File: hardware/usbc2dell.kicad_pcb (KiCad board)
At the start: 2 copper layers, 39.5 x 26.5 mm, 27 parts, among them J1 TYPE-C-31-M-17, J2 WJ15EDGRC-3.81-3P, Q1 DOD50P06, Q2 MMBT5551, SW1 DSWB04LHGET, U1 ATtiny1616-M, U2 FUSB302BMPX, U3 L7805, U4 SRV05-4

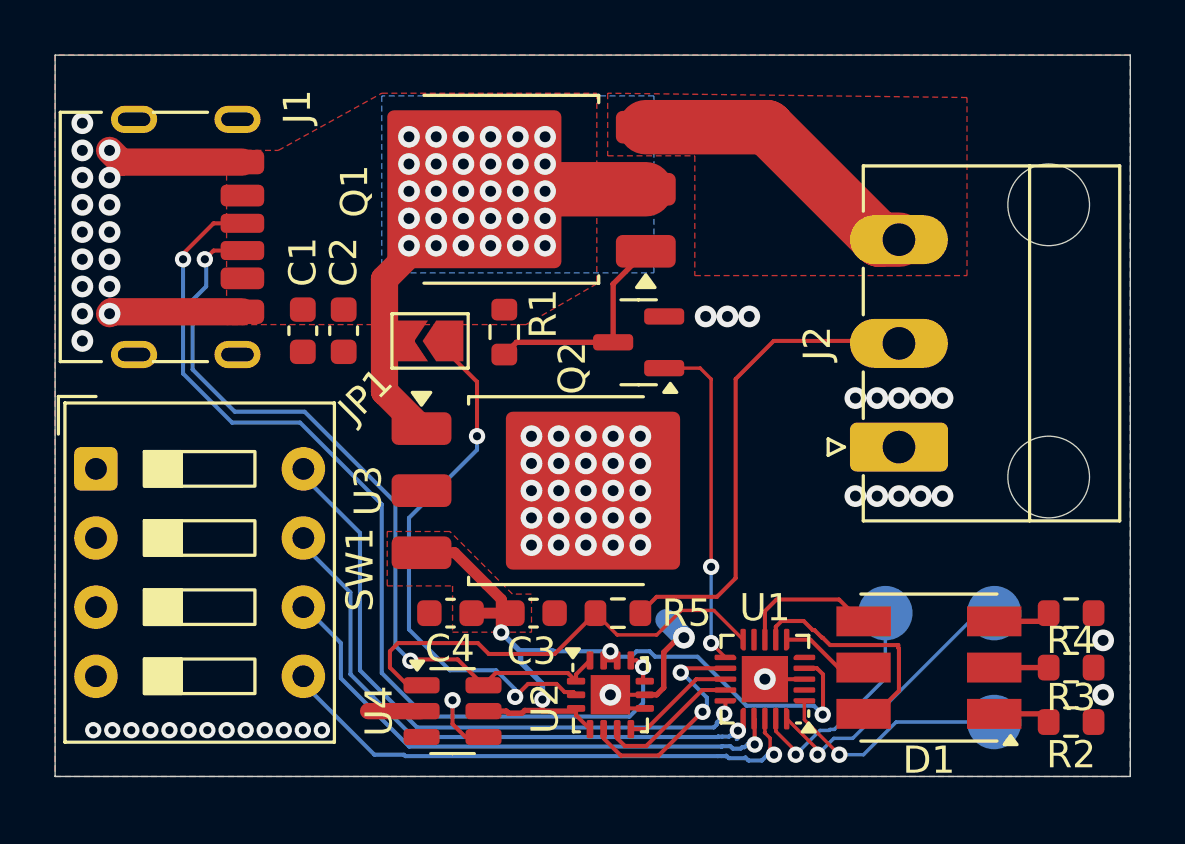
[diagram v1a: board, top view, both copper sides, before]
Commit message: nicer traces + mosfet still fucked
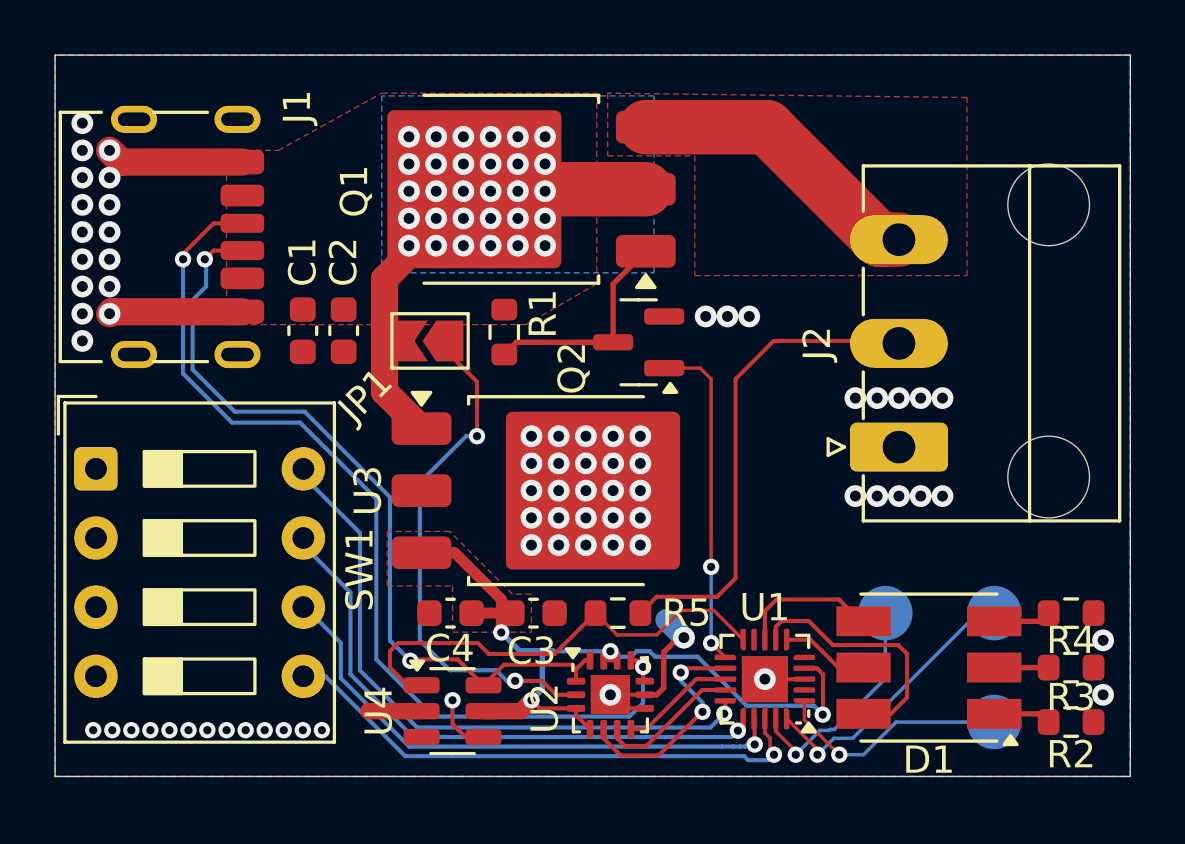
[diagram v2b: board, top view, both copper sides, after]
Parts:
- Q1: value DOD50P06 -> ~
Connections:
- Q1 pad 2: /Vout -> VBUS
- Q1 pad 3: VBUS -> /Vout
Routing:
- net /LED_R: track 8.77 -> 9.34 mm
- net Net-(JP1-A): track 19.7 -> 19.2 mm

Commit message: attempt to fix mosfet
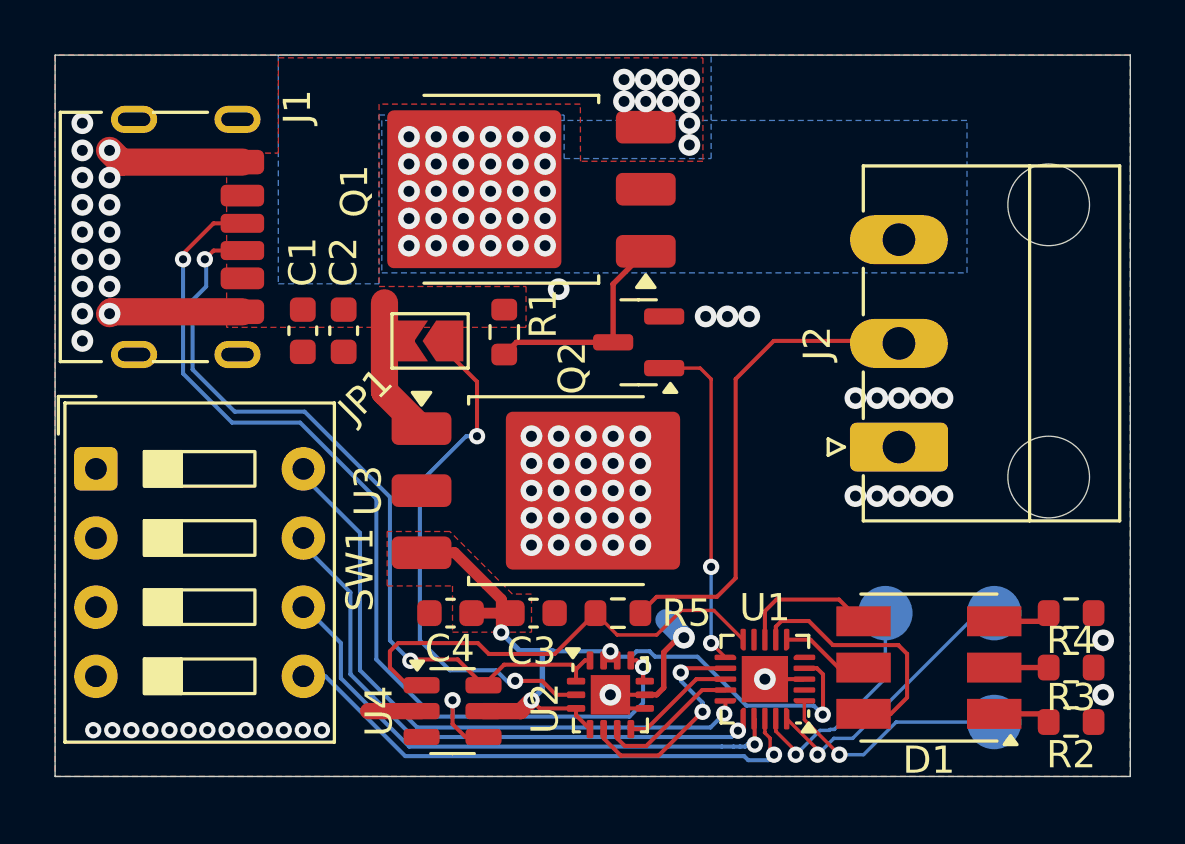
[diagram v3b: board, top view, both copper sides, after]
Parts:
- Q1: value ~ -> DOD50P06
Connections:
- Q1 pad 2: VBUS -> /Vout
- Q1 pad 3: /Vout -> VBUS
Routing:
- net VBUS: track 17.0 -> 5.18 mm, vias 30 -> 10
- net /Vout: track 11.0 -> 0.00 mm, vias 0 -> 30
- net GND: vias 72 -> 73
- added copper zone on B.Cu, net /Vout
- removed copper zone on F.Cu, net /Vout

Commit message: actually fix mosfet
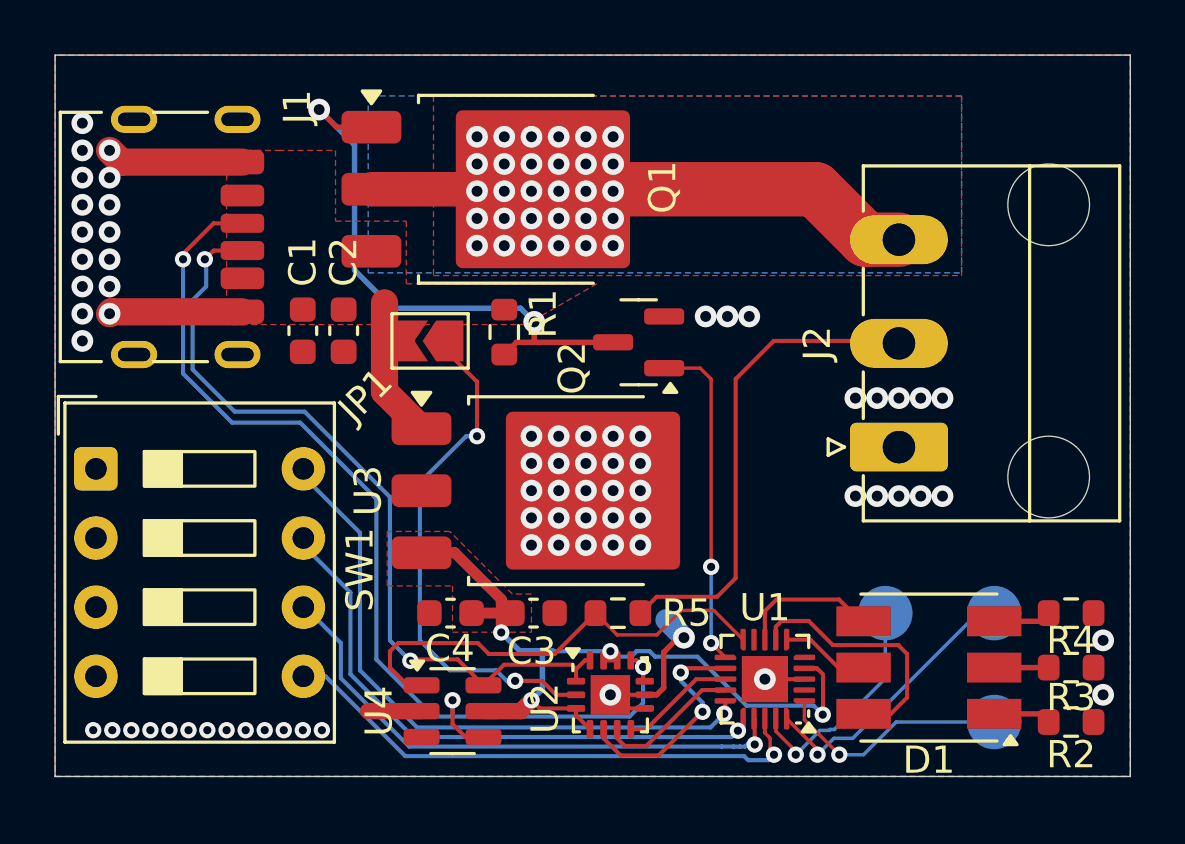
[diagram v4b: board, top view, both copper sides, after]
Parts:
- turned Q1 to 0 degrees
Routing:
- net /Vout: track 0.00 -> 20.1 mm
- net /PWR_GATE: track 8.03 -> 21.0 mm, vias 0 -> 2
- net VBUS: vias 10 -> 0
- net GND: vias 73 -> 72
- added copper zone on F.Cu, net /Vout
- removed copper zone on B.Cu, net VBUS

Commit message: idk
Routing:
- net /PWR_GATE: track 21.0 -> 22.0 mm

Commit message: correct 7805 part num
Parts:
- U3: value L7805 -> MC7805CDTRKG

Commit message: thermals
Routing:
- net GND: vias 72 -> 92

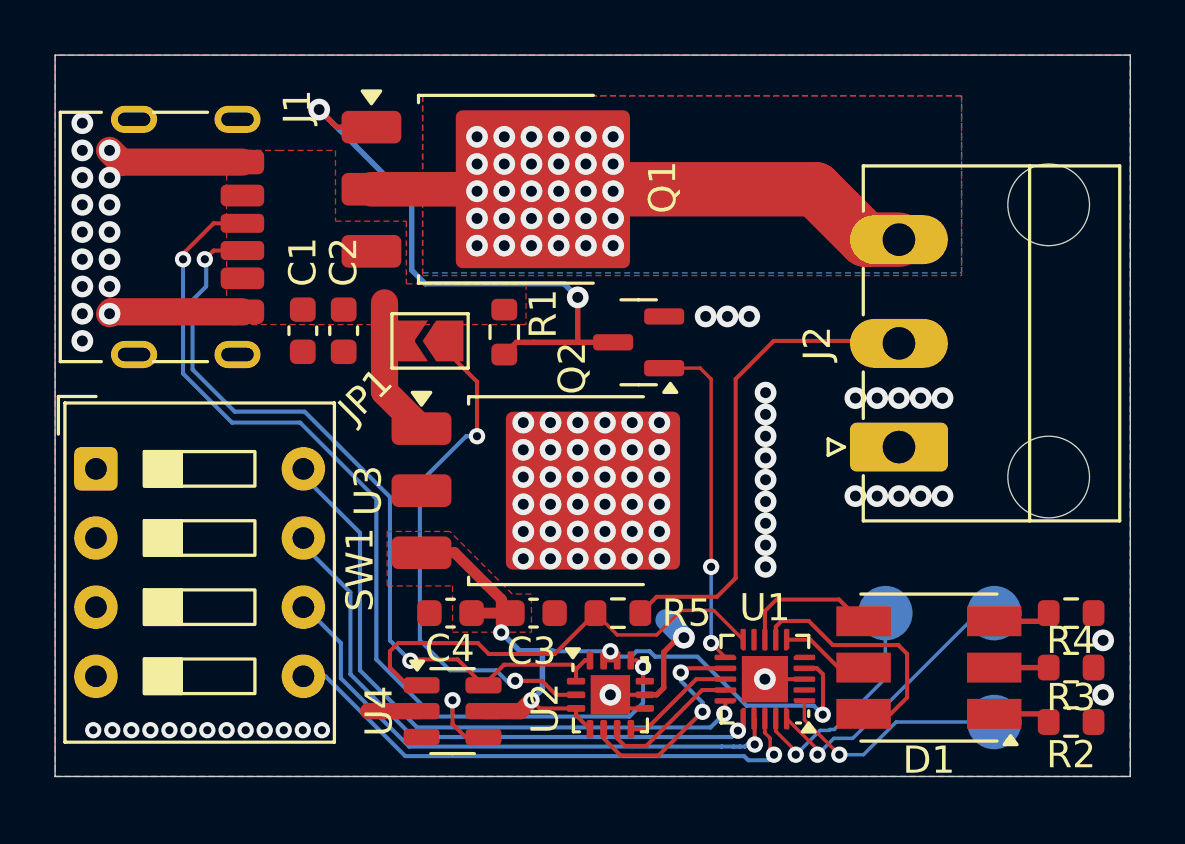
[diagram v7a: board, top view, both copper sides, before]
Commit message: layout changes, thermals +  ampacity
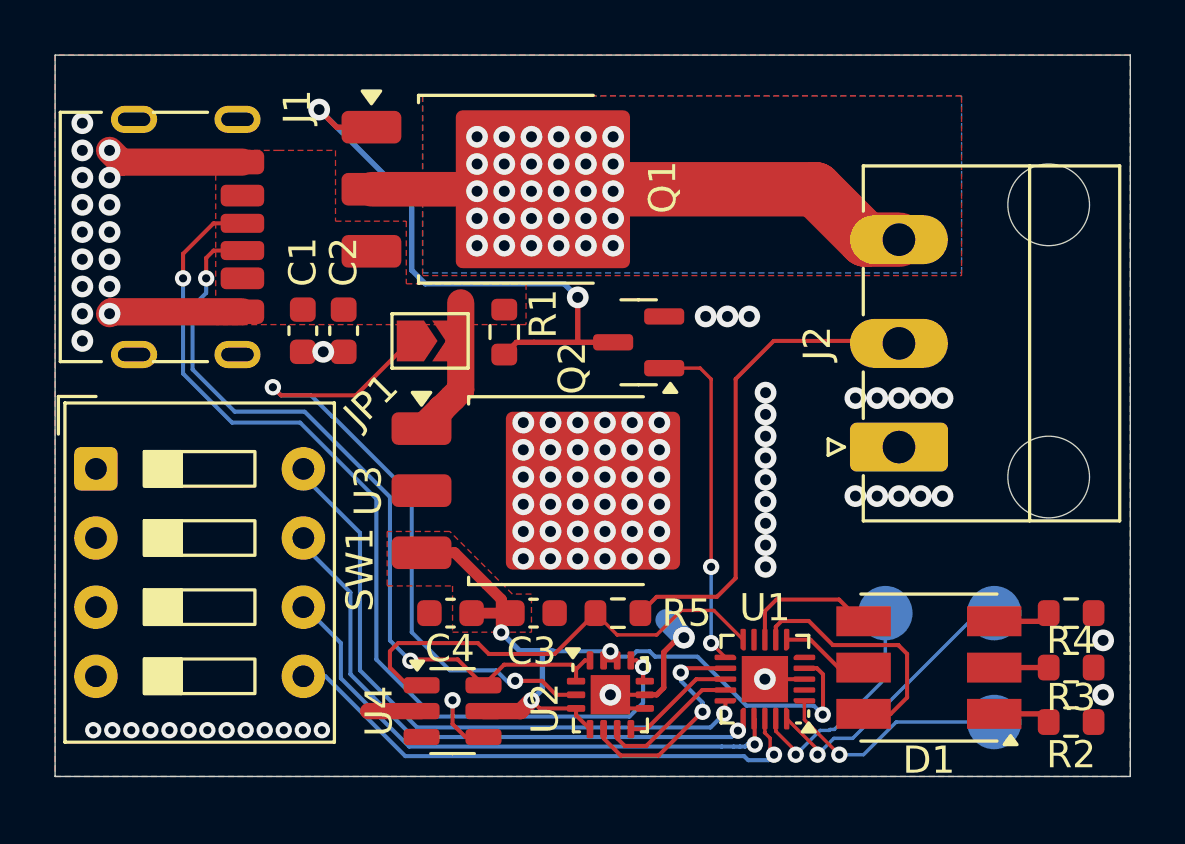
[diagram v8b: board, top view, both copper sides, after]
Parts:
- turned JP1 to 0 degrees
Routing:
- net Net-(JP1-A): track 19.2 -> 24.9 mm
- net GND: vias 92 -> 93
